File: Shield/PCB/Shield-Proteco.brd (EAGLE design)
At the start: 100 x 80 mm, 28 parts

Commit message: Avance shield y correccion librerias
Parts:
- removed BT-PROG: HC-05-PROG, hc-xx:HC-05-PROG
- removed LINE-SENSOR: CNY70-ARRAY, Sensores:CNY70-ARRAY
- removed M-LEFT, M-RIGHT: POLOLU-MICROMOTOR, Motores:JST
- removed SHARP-LEFT, SHARP-MIDD, SHARP-RIGHT: SHARP, Sensores:SHARP
- added ARDUINO-MEGA: ARDUINO_MEGA, Arduino:ARDUINO-MEGA
- added LED1, LED2, LED3, LED4, LED5: (no value), led:CHIPLED_1206
- added R10, R11, R12, R13, R14: (no value), rcl:M1206
- added U$10, U$11, U$9: SHARP, Sensores:SHARP
- added U$12: CNY70-ARRAY, Sensores:CNY70-ARRAY
- added U$13: HC-05-PROG, hc-xx:HC-05-PROG
- added U$14: TFT_ARDUINO-UNO-MEGA, TFT:TFT-ARDUINO-UNO-MEGA
- added U$15: ACELEROMETER-MPU6050-JST, Sensores:ACELEROMETER-MPU6050-JST
- added U$16, U$17: SERVOMOTORES, Motores:SERVO
- added U$18: SLIDE-3, Interruptores:SLIDE-3
- added U$3, U$6: TB6612FNG, Driver-Motor:TB6612FNG
- added U$7, U$8: POLOLU-MICROMOTOR, Motores:JST
- U$1: value ARDUINO_MEGA -> SERVOMOTORES; device Arduino:ARDUINO-MEGA -> Motores:SERVO
- moved R1 99.2 mm to (101.6, 26.7), turned to 0 degrees
- moved R3 91.6 mm to (101.6, 22.2), turned to 270 degrees
- moved SW2 91.2 mm to (21.0, 73.7)
- moved R2 79.7 mm to (85.7, 22.2), turned to 270 degrees
- moved R4 79.1 mm to (88.9, 35.6)
- moved S1 75.0 mm to (88.3, 66.7), turned to 0 degrees
- moved SW1 69.4 mm to (77.5, 6.99), turned to 180 degrees
- moved S3 68.2 mm to (88.3, 74.3), turned to 0 degrees
- moved U$2 65.7 mm to (78.1, 76.8), turned to 0 degrees
- moved S2 62.0 mm to (88.9, 59.1), turned to 0 degrees
- moved R5 57.4 mm to (90.2, 40.6)
- moved SG1 50.2 mm to (62.2, 48.9)
- moved R7 47.9 mm to (101.6, 15.9), turned to 90 degrees
- moved S4 43.2 mm to (88.9, 51.4), turned to 0 degrees
- moved R6 42.6 mm to (85.1, 14.6), turned to 90 degrees
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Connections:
- new net N$17: U$15.SCL
- new net N$18: U$15.SDA
- new net N$19: U$15.XDA
- new net N$20: U$15.XCL
- new net N$21: U$15.ADO
- new net N$22: U$15.INT
- new net N$23: LED1.C, R10.2
- new net N$24: LED2.C, R11.2
- new net N$25: LED3.C, R12.2
- new net N$26: LED4.C, R13.2
- new net N$27: U$14.0-RX0
- new net N$28: U$14.3V3
- new net N$29: U$14.5V_1, U$18.P2
- new net N$30: U$14.GND_2
- new net N$31: U$14.GND_1
- new net N$32: U$14.VIN
- new net N$33: U$14.A0
- new net N$34: U$14.A1
- new net N$35: U$14.A2
- new net N$36: U$14.A3
- new net N$37: U$14.A4
- new net N$38: U$14.A5
- new net N$39: ARDUINO-MEGA.3V3
- new net N$40: ARDUINO-MEGA.5V_1
- new net N$41: ARDUINO-MEGA.GND_2
- new net N$42: ARDUINO-MEGA.GND_1
- new net N$43: ARDUINO-MEGA.VIN
- new net N$44: ARDUINO-MEGA.A0
- new net N$45: ARDUINO-MEGA.A1
- new net N$46: ARDUINO-MEGA.A2
- new net N$47: ARDUINO-MEGA.A3
- new net N$48: ARDUINO-MEGA.A4
- new net N$49: ARDUINO-MEGA.A5
- new net N$50: ARDUINO-MEGA.A6
- new net N$51: ARDUINO-MEGA.A7
- new net N$52: ARDUINO-MEGA.A8
- new net N$53: ARDUINO-MEGA.A9
- new net N$54: ARDUINO-MEGA.A10
- new net N$55: ARDUINO-MEGA.A11
- new net N$56: ARDUINO-MEGA.A12
- new net N$57: ARDUINO-MEGA.A13
- new net N$58: ARDUINO-MEGA.A14
- new net N$59: ARDUINO-MEGA.A15
- new net N$60: U$14.1-TX0
- new net N$61: U$14.2
- new net N$62: U$14.3
- new net N$63: U$14.4
- new net N$64: U$14.5
- new net N$65: U$14.6
- new net N$66: U$14.7
- new net N$67: U$14.AREF
- new net N$68: U$14.GND
- new net N$70: U$14.12
- new net N$71: U$14.11
- new net N$72: U$14.10
- new net N$73: U$14.9
- new net N$74: U$14.8
- new net N$75: U$1.SIGNAL
- new net N$76: U$16.SIGNAL
- new net N$77: U$17.SIGNAL
- new net N$78: ARDUINO-MEGA.SCL
- new net N$79: ARDUINO-MEGA.SDA
- new net N$80: ARDUINO-MEGA.AREF
- new net N$81: ARDUINO-MEGA.GND
- new net SD_SCK: ARDUINO-MEGA.13, U$14.13
- net 6V-DC-3A: now also U$3.VM, U$6.VM; no longer M-LEFT.VCC, M-RIGHT.VCC
- net GND: now also R10.1, R11.1, R12.1, R13.1, R14.1, U$1.GND, U$10.GND, U$11.GND, U$12.GND, U$13.GND, U$15.GND, U$16.GND, U$17.GND, U$3.GND, U$3.GND_1, U$3.GND_2, U$6.GND, U$6.GND_1, U$6.GND_2, U$7.GND, U$8.GND, U$9.GND; no longer BT-PROG.GND, LINE-SENSOR.GND, M-LEFT.GND, M-RIGHT.GND, SHARP-LEFT.GND, SHARP-MIDD.GND, SHARP-RIGHT.GND
- net N$16: now also U$13.RESET; no longer BT-PROG.RESET
- net N$7: now also U$9.DIST; no longer SHARP-LEFT.DIST
- net N$8: now also U$10.DIST; no longer SHARP-MIDD.DIST
- net N$9: now also U$11.DIST; no longer SHARP-RIGHT.DIST
- net RESET: now also ARDUINO-MEGA.RESET, U$14.RESET
- net RX0: now also U$13.RXD; no longer BT-PROG.RXD
- net SCD: now also U$12.SCD; no longer LINE-SENSOR.SCD
- net SCI: now also U$12.SCI; no longer LINE-SENSOR.SCI
- net SF: now also U$12.SF; no longer LINE-SENSOR.SF
- net SID: now also U$12.SID; no longer LINE-SENSOR.SID
- net SII: now also U$12.SII; no longer LINE-SENSOR.SII
- net SSD: now also U$12.SSD; no longer LINE-SENSOR.SSD
- net SSI: now also U$12.SSI; no longer LINE-SENSOR.SSI
- net TX0: now also U$13.TXD; no longer BT-PROG.TXD
- net VCC: now also U$1.VCC, U$10.VCC, U$11.VCC, U$12.VCC, U$13.VCC, U$15.VCC, U$16.VCC, U$17.VCC, U$18.COM, U$3.VCC, U$6.VCC, U$7.VCC, U$8.VCC, U$9.VCC; no longer BT-PROG.VCC, LINE-SENSOR.VCC, SHARP-LEFT.VCC, SHARP-MIDD.VCC, SHARP-RIGHT.VCC
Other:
- board size 100 x 80 mm -> 106.3 x 81.3 mm

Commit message: Avance Shield
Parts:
- removed SG1: F/CM12P, buzzer:F/CM12P
- removed T1: (no value), transistor:TO92-CBE
- added BC547: (no value), transistor:TO92-CBE
- added BUZZER: F/CM12P, buzzer:F/CM12P
- added D1, D2: (no value), zetex:SOD323
- added LED6: (no value), led:CHIPLED_1206
- added R15: (no value), rcl:M1206
- added SHARP-LEFT, SHARP-MIDDLE: SHARP, Sensores:SHARP
- U$10: value SHARP -> SERVOMOTORES; device Sensores:SHARP -> Motores:SERVO
- U$9: value SHARP -> SENSOR-MISCELANEOUS; device Sensores:SHARP -> Sensores:SENSOR-MISCELANEOUS
- moved U$9 79.9 mm to (98.4, 61.0), turned to 90 degrees
- moved U$10 72.5 mm to (-17.8, -6.99)
- moved U$4 22.9 mm to (62.2, 32.4)
- moved U$5 22.9 mm to (62.2, 52.1)
- moved LED5 9.09 mm to (86.4, 43.2)
- moved U$1 3.24 mm to (27.3, 10.8)
- moved U$17 2.62 mm to (5.71, 10.8)
- moved U$16 2.62 mm to (16.5, 10.8)
- renumbered U$11 to SHARP-RIGHT, U$13 to HC-05
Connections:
- new net LED1: LED1.A
- new net LED2: LED2.A
- new net LED3: LED3.A
- new net LED4: LED4.A
- new net LED5: LED5.A
- new net N$100: U$3.AO2, U$3.BO2
- new net N$101: U$3.AO1, U$3.BO1
- new net N$102: U$7.OUTB
- new net N$103: U$7.OUTA
- new net N$104: U$7.M2
- new net N$105: U$7.M1
- new net N$106: U$8.OUTA
- new net N$107: U$8.OUTB
- new net N$108: U$8.M2
- new net N$109: U$8.M1
- new net N$110: U$9.3V3
- new net N$111: ARDUINO-MEGA.12
- new net N$112: ARDUINO-MEGA.11
- new net N$113: ARDUINO-MEGA.10
- new net N$114: ARDUINO-MEGA.9
- new net N$115: ARDUINO-MEGA.8
- new net N$116: ARDUINO-MEGA.7
- new net N$117: ARDUINO-MEGA.6
- new net N$69: U$9.1
- new net N$82: U$9.2
- new net N$83: U$9.3
- new net N$84: U$9.4
- new net N$85: U$9.5
- new net N$86: U$9.6
- new net N$87: U$9.7
- new net N$88: LED5.C, R14.2
- new net N$89: LED6.C, R15.2
- new net N$90: D2.2, HC-05.TXD
- new net N$91: D1.1, HC-05.RXD
- new net N$92: U$6.AI1, U$6.BI1
- new net N$93: U$6.AI2, U$6.BI2
- new net N$94: U$6.AO2, U$6.BO2
- new net N$95: U$6.AO1, U$6.BO1
- new net N$96: U$6.PWMA, U$6.PWMB
- new net N$97: U$3.AI1, U$3.BI1
- new net N$98: U$3.AI2, U$3.BI2
- new net N$99: U$3.PWMA, U$3.PWMB
- net GND: now also BC547.E, R15.1, SHARP-LEFT.GND, SHARP-MIDDLE.GND; no longer T1.E
- net N$10: now also S2.4
- net N$11: now also S1.4
- net N$12: now also S3.4
- net N$13: now also S4.4
- net N$5: now also BC547.C, BUZZER.-; no longer SG1.-, T1.C
- net N$6: now also BC547.B; no longer T1.B
- net N$7: now also SHARP-LEFT.DIST; no longer U$9.DIST
- net N$77: now also U$10.SIGNAL
- net N$8: now also SHARP-MIDDLE.DIST; no longer U$10.DIST
- net RX0: now also D2.1; no longer HC-05.RXD
- net TX0: now also D1.2; no longer HC-05.TXD
- net VCC: now also BUZZER.+, LED6.A, SHARP-LEFT.VCC, SHARP-MIDDLE.VCC; no longer SG1.+

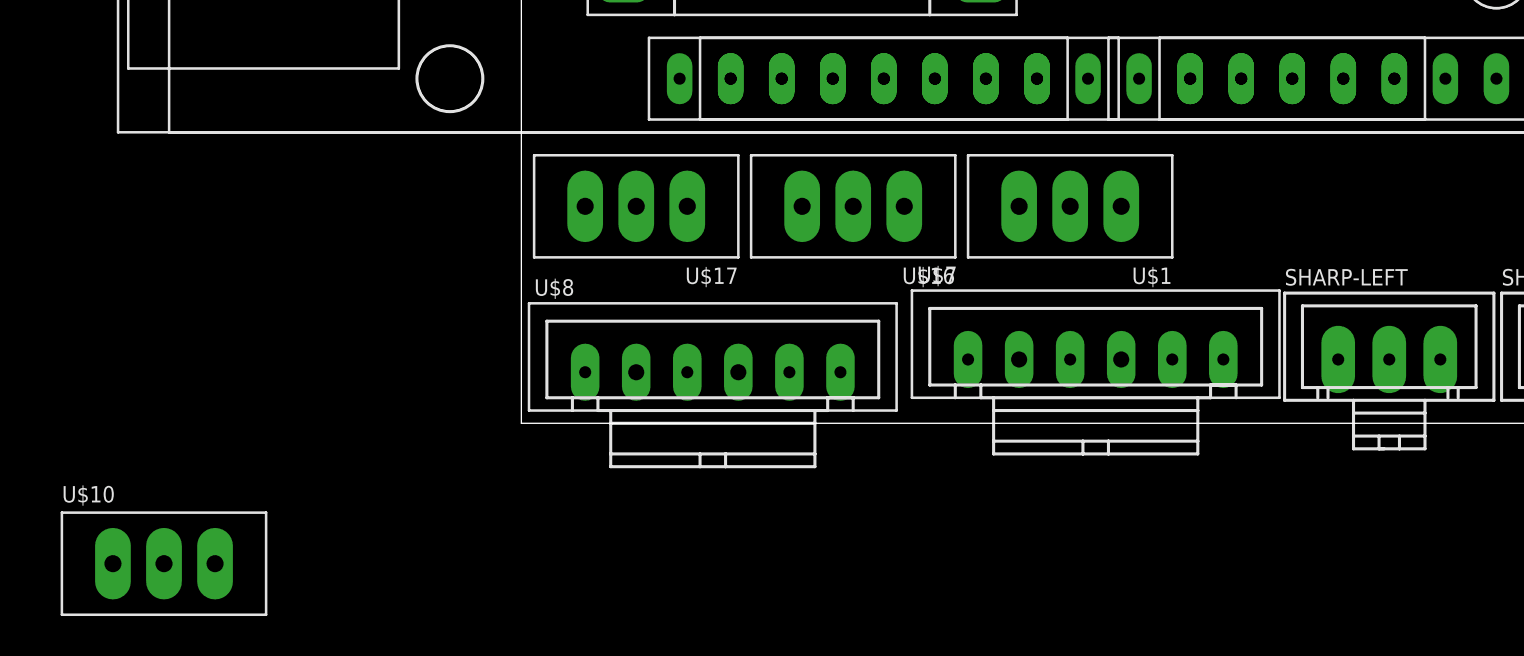
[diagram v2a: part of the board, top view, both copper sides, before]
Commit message: Se agregan elementos del diseño mecánico
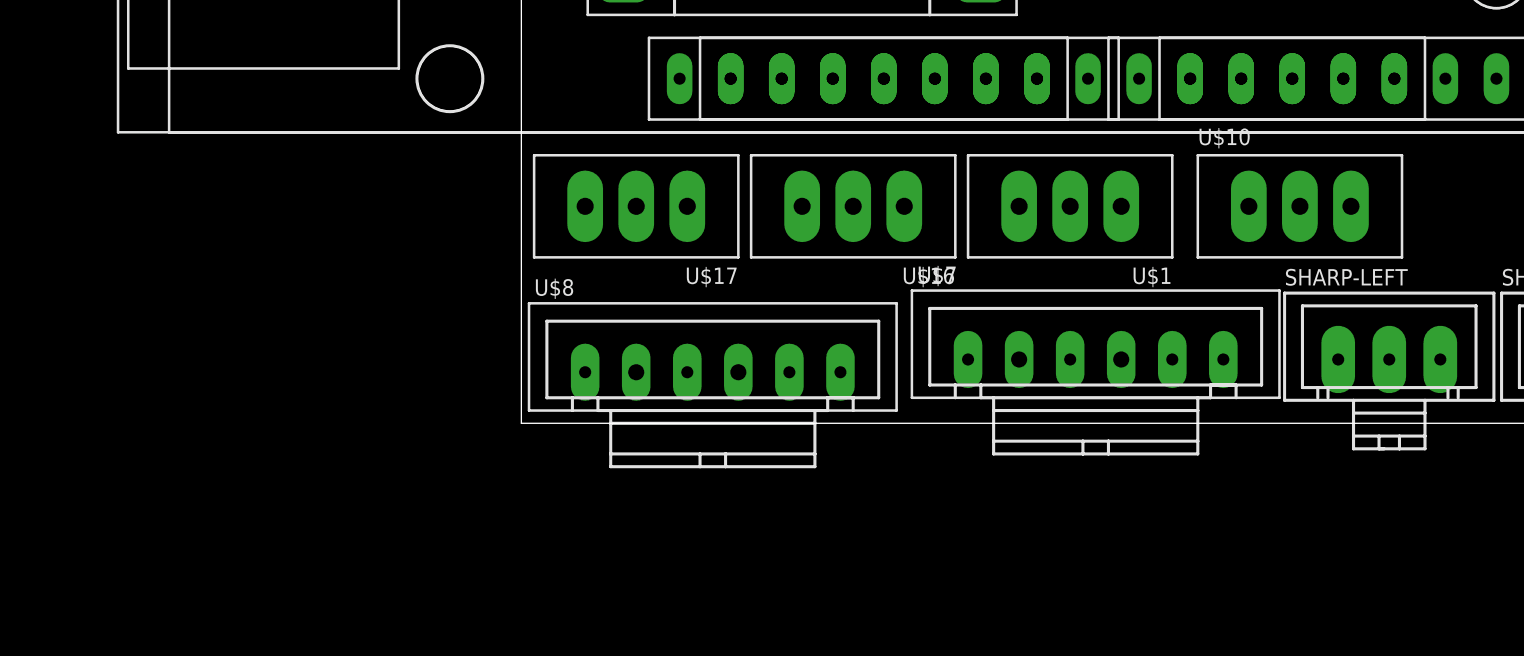
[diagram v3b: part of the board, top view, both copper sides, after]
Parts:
- moved U$10 59.2 mm to (38.7, 10.8)
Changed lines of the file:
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@@
 <?xml version="1.0" encoding="utf-8"?>
 <!DOCTYPE eagle SYSTEM "eagle.dtd">
-<eagle version="9.1.0">
+<eagle version="9.1.3">
 <drawing>
 <settings>
@@
 <attribute name="OC_NEWARK" value="79R6078" x="97.155" y="47.625" size="1.778" layer="27" display="off"/>
 </element>
-<element name="U$10" library="Motores" package="SERVO" value="SERVOMOTORES" x="-17.78" y="-6.985"/>
+<element name="U$10" library="Motores" package="SERVO" value="SERVOMOTORES" x="38.735" y="10.795"/>
 </elements>
 <signals>
@@
 <wire x1="52.07" y1="38.735" x2="31.115" y2="52.07" width="0" layer="19" extent="1-1"/>
 <wire x1="12.065" y1="71.12" x2="31.115" y2="52.07" width="0" layer="19" extent="1-1"/>
-<wire x1="-17.78" y1="-6.985" x2="5.715" y2="10.795" width="0" layer="19" extent="1-1"/>
+<wire x1="38.735" y1="10.795" x2="5.715" y2="10.795" width="0" layer="19" extent="1-1"/>
 </signal>
 <signal name="N$1">
@@
 <wire x1="53.975" y1="3.175" x2="43.18" y2="3.175" width="0" layer="19" extent="1-1"/>
 <wire x1="64.77" y1="3.175" x2="53.975" y2="3.175" width="0" layer="19" extent="1-1"/>
-<wire x1="-15.24" y1="-6.985" x2="3.175" y2="2.54" width="0" layer="19" extent="1-1"/>
+<wire x1="41.275" y1="10.795" x2="3.175" y2="2.54" width="0" layer="19" extent="1-1"/>
 <wire x1="41.91" y1="76.835" x2="22.86" y2="60.96" width="0" layer="19" extent="1-1"/>
 <wire x1="70.485" y1="76.835" x2="41.91" y2="76.835" width="0" layer="19" extent="1-1"/>
@@
 <contactref element="U$17" pad="SIGNAL"/>
 <contactref element="U$10" pad="SIGNAL"/>
-<wire x1="8.255" y1="10.795" x2="-20.32" y2="-6.985" width="0" layer="19" extent="1-1"/>
+<wire x1="8.255" y1="10.795" x2="36.195" y2="10.795" width="0" layer="19" extent="1-1"/>
 </signal>
 <signal name="N$29">
